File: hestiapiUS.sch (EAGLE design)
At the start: 24 parts, among them U1 RPI-ZERO, U2 ULN2003AD, U3 LM2675MX-5.0/NOPBM08A-L, X1 MKDSN1,5/2-5,08, X2 MKDSN1,5/6-5,08

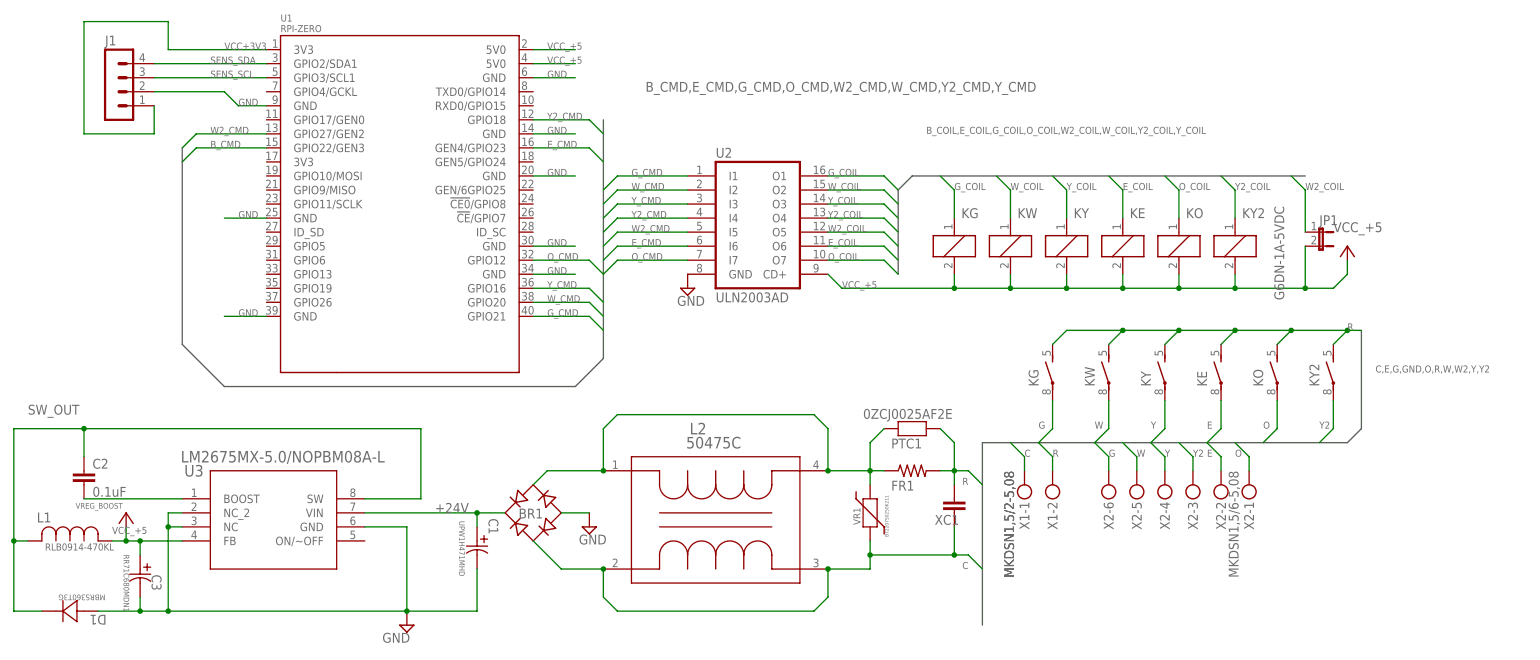
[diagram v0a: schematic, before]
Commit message: fix library pathing and add library
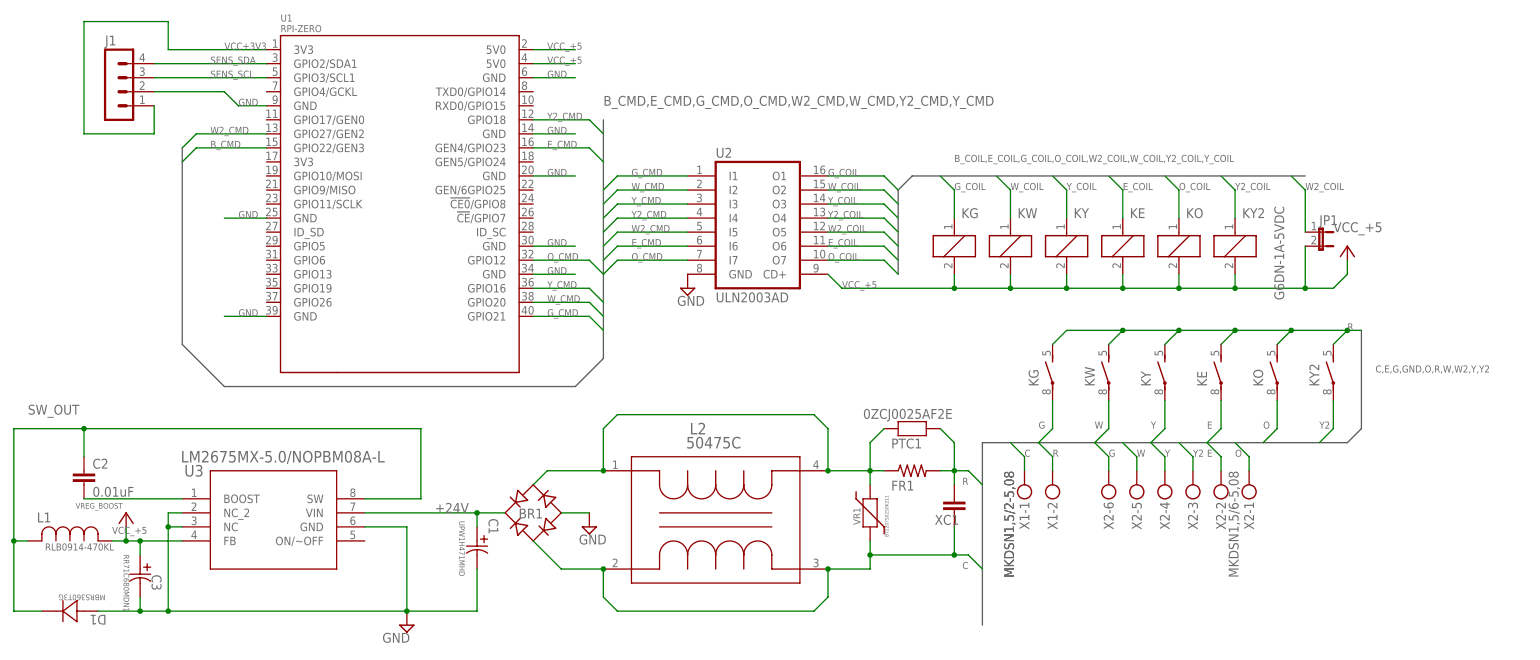
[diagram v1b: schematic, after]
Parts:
- BR1: device rectifier:DF06S -> hestiapiUS:DF06S
- C1: device obbgood:UPW1H471MHD -> hestiapiUS:UPW1H471MHD
- C2: value 0.1uF -> 0.01uF; device SparkFun-Capacitors:0.1UF-0603-25V-(+80/-20%) -> hestiapiUS:0.01UF-0603-25V-(+80/-20%)
- C3: device obbgood:RR71C680MDN1 -> hestiapiUS:RR71C680MDN1
- D1: device obbgood:MBRS360T3G -> hestiapiUS:MBRS360T3G
- J1: device con-lstb:MA04-1 -> hestiapiUS:MA04-1
- JP1: device jumper:JP1E -> hestiapiUS:JP1E
- KE, KG, KO, KW, KY, KY2: device obbgood:G6DN-1A-5VDC -> hestiapiUS:G6DN-1A-5VDC
- L1: device obbgood:RLB0914-470KL -> hestiapiUS:RLB0914-470KL
- L2: device obbgood:50475C -> hestiapiUS:50475C
- PTC1: device obbgood:0ZCJ0025AF2E -> hestiapiUS:0ZCJ0025AF2E
- U1: device RPI-Zero:RPI-ZERO -> hestiapiUS:RPI-ZERO
- U2: device uln-udn:ULN2003AD -> hestiapiUS:ULN2003AD
- U3: device obbgood:LM2675MX-5.0/NOPBM08A-L -> hestiapiUS:LM2675MX-5.0/NOPBM08A-L
- VR1: device obbgood:B72207S0250K211 -> hestiapiUS:B72207S0250K211
- X1: device obbgood:MKDSN1,5/2-5,08 -> hestiapiUS:MKDSN1,5/2-5,08
- X2: device obbgood:MKDSN1,5/6-5,08 -> hestiapiUS:MKDSN1,5/6-5,08
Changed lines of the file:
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@@
 </classes>
 <parts>
-<part name="KG" library="obbgood" deviceset="G6DN?*" device="-1A-" package3d_urn="urn:adsk.eagle:package:24538/1" technology="5VDC" value="G6DN-1A-5VDC"/>
-<part name="KW" library="obbgood" deviceset="G6DN?*" device="-1A-" package3d_urn="urn:adsk.eagle:package:24538/1" technology="5VDC" value="G6DN-1A-5VDC"/>
-<part name="KY" library="obbgood" deviceset="G6DN?*" device="-1A-" package3d_urn="urn:adsk.eagle:package:24538/1" technology="5VDC" value="G6DN-1A-5VDC"/>
-<part name="KE" library="obbgood" deviceset="G6DN?*" device="-1A-" package3d_urn="urn:adsk.eagle:package:24538/1" technology="5VDC" value="G6DN-1A-5VDC"/>
-<part name="KO" library="obbgood" deviceset="G6DN?*" device="-1A-" package3d_urn="urn:adsk.eagle:package:24538/1" technology="5VDC" value="G6DN-1A-5VDC"/>
-<part name="KY2" library="obbgood" deviceset="G6DN?*" device="-1A-" package3d_urn="urn:adsk.eagle:package:24538/1" technology="5VDC" value="G6DN-1A-5VDC"/>
-<part name="U1" library="RPI-Zero" deviceset="RPI-ZERO" device=""/>
-<part name="U2" library="uln-udn" library_urn="urn:adsk.eagle:library:407" deviceset="ULN2003A" device="D" package3d_urn="urn:adsk.eagle:package:923/2"/>
+<part name="KG" library="hestiapiUS" deviceset="G6DN?*" device="-1A-" package3d_urn="urn:adsk.eagle:package:24538/1" technology="5VDC" value="G6DN-1A-5VDC"/>
+<part name="KW" library="hestiapiUS" deviceset="G6DN?*" device="-1A-" package3d_urn="urn:adsk.eagle:package:24538/1" technology="5VDC" value="G6DN-1A-5VDC"/>
+<part name="KY" library="hestiapiUS" deviceset="G6DN?*" device="-1A-" package3d_urn="urn:adsk.eagle:package:24538/1" technology="5VDC" value="G6DN-1A-5VDC"/>
+<part name="KE" library="hestiapiUS" deviceset="G6DN?*" device="-1A-" package3d_urn="urn:adsk.eagle:package:24538/1" technology="5VDC" value="G6DN-1A-5VDC"/>
+<part name="KO" library="hestiapiUS" deviceset="G6DN?*" device="-1A-" package3d_urn="urn:adsk.eagle:package:24538/1" technology="5VDC" value="G6DN-1A-5VDC"/>
+<part name="KY2" library="hestiapiUS" deviceset="G6DN?*" device="-1A-" package3d_urn="urn:adsk.eagle:package:24538/1" technology="5VDC" value="G6DN-1A-5VDC"/>
+<part name="U1" library="hestiapiUS" deviceset="RPI-ZERO" device=""/>
+<part name="U2" library="hestiapiUS" deviceset="ULN2003A" device="D" package3d_urn="urn:adsk.eagle:package:923/2"/>
 <part name="SUPPLY1" library="supply2" library_urn="urn:adsk.eagle:library:372" deviceset="GND" device=""/>
-<part name="J1" library="con-lstb" library_urn="urn:adsk.eagle:library:162" deviceset="MA04-1" device="" package3d_urn="urn:adsk.eagle:package:8337/1"/>
-<part name="BR1" library="rectifier" library_urn="urn:adsk.eagle:library:336" deviceset="DF*S" device="" package3d_urn="urn:adsk.eagle:package:23903/1" technology="06"/>
-<part name="X2" library="obbgood" deviceset="MKDSN1,5/6-5,08" device="" package3d_urn="urn:adsk.eagle:package:9634/1"/>
-<part name="X1" library="obbgood" deviceset="MKDSN1,5/2-5,08" device="" package3d_urn="urn:adsk.eagle:package:9630/1"/>
+<part name="J1" library="hestiapiUS" deviceset="MA04-1" device="" package3d_urn="urn:adsk.eagle:package:8337/1"/>
+<part name="BR1" library="hestiapiUS" deviceset="DF*S" device="" package3d_urn="urn:adsk.eagle:package:23903/1" technology="06"/>
+<part name="X2" library="hestiapiUS" deviceset="MKDSN1,5/6-5,08" device="" package3d_urn="urn:adsk.eagle:package:9634/1"/>
+<part name="X1" library="hestiapiUS" deviceset="MKDSN1,5/2-5,08" device="" package3d_urn="urn:adsk.eagle:package:9630/1"/>
 <part name="SUPPLY2" library="supply2" library_urn="urn:adsk.eagle:library:372" deviceset="GND" device=""/>
 <part name="SUPPLY4" library="supply2" library_urn="urn:adsk.eagle:library:372" deviceset="GND" device=""/>
-<part name="C1" library="obbgood" deviceset="UPW1H471MHD" device=""/>
-<part name="U3" library="obbgood" deviceset="LM2675MX-5.0/NOPB" device="M08A-L"/>
-<part name="D1" library="obbgood" deviceset="MBRS360T3G" device=""/>
-<part name="L1" library="obbgood" deviceset="RLB0914-470KL" device=""/>
-<part name="C2" library="SparkFun-Capacitors" library_urn="urn:adsk.eagle:library:510" deviceset="0.1UF" device="-0603-25V-(+80/-20%)" package3d_urn="urn:adsk.eagle:package:37414/1" value="0.1uF"/>
+<part name="C1" library="hestiapiUS" deviceset="UPW1H471MHD" device=""/>
+<part name="U3" library="hestiapiUS" deviceset="LM2675MX-5.0/NOPB" device="M08A-L"/>
+<part name="D1" library="hestiapiUS" deviceset="MBRS360T3G" device=""/>
+<part name="L1" library="hestiapiUS" deviceset="RLB0914-470KL" device=""/>
+<part name="C2" library="hestiapiUS" deviceset="0.01UF" device="-0603-25V-(+80/-20%)" package3d_urn="urn:adsk.eagle:package:37414/1" value="0.01uF"/>
 <part name="P+1" library="supply1" library_urn="urn:adsk.eagle:library:371" deviceset="VCC" device=""/>
-<part name="C3" library="obbgood" deviceset="RR71C680MDN1" device=""/>
+<part name="C3" library="hestiapiUS" deviceset="RR71C680MDN1" device=""/>
 <part name="P+2" library="supply1" library_urn="urn:adsk.eagle:library:371" deviceset="VCC" device=""/>
-<part name="JP1" library="jumper" library_urn="urn:adsk.eagle:library:252" deviceset="JP1E" device="" package3d_urn="urn:adsk.eagle:package:15455/1"/>
+<part name="JP1" library="hestiapiUS" deviceset="JP1E" device="" package3d_urn="urn:adsk.eagle:package:15455/1"/>
 <part name="FR1" library="rcl" library_urn="urn:adsk.eagle:library:334" deviceset="R-US_" device="0207/12" package3d_urn="urn:adsk.eagle:package:23489/1"/>
-<part name="PTC1" library="obbgood" deviceset="0ZCJ0025AF2E" device=""/>
+<part name="PTC1" library="hestiapiUS" deviceset="0ZCJ0025AF2E" device=""/>
 <part name="XC1" library="rcl" library_urn="urn:adsk.eagle:library:334" deviceset="C-EU" device="025-024X044" package3d_urn="urn:adsk.eagle:package:23630/1"/>
-<part name="VR1" library="obbgood" deviceset="B72207S0250K211" device=""/>
-<part name="L2" library="obbgood" deviceset="50475C" device=""/>
+<part name="VR1" library="hestiapiUS" deviceset="B72207S0250K211" device=""/>
+<part name="L2" library="hestiapiUS" deviceset="50475C" device=""/>
 </parts>
 <sheets>
@@
 <segment>
 <wire x1="-15.24" y1="33.02" x2="-15.24" y2="76.2" width="0.762" layer="92"/>
-<label x="-7.62" y="81.28" size="1.778" layer="95"/>
+<label x="-15.24" y="78.74" size="1.778" layer="95"/>
 <wire x1="-15.24" y1="33.02" x2="-20.32" y2="27.94" width="0.762" layer="92"/>
 <wire x1="-20.32" y1="27.94" x2="-83.82" y2="27.94" width="0.762" layer="92"/>
@@
 <segment>
 <wire x1="38.1" y1="63.5" x2="38.1" y2="48.26" width="0.762" layer="92"/>
-<label x="43.18" y="73.66" size="1.27" layer="95"/>
+<label x="48.26" y="68.58" size="1.27" layer="95"/>
 <wire x1="38.1" y1="63.5" x2="40.64" y2="66.04" width="0.762" layer="92"/>
 <wire x1="40.64" y1="66.04" x2="111.76" y2="66.04" width="0.762" layer="92"/>
